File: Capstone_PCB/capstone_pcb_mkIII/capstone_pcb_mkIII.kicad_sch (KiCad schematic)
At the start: 18 parts, among them J1 DISPLAY_HEADER, J2 UART_TX, J3 UART_RX, J4 GND, SW1 SW_Push, SW2 SW_Push, U1 TPS62125DSG

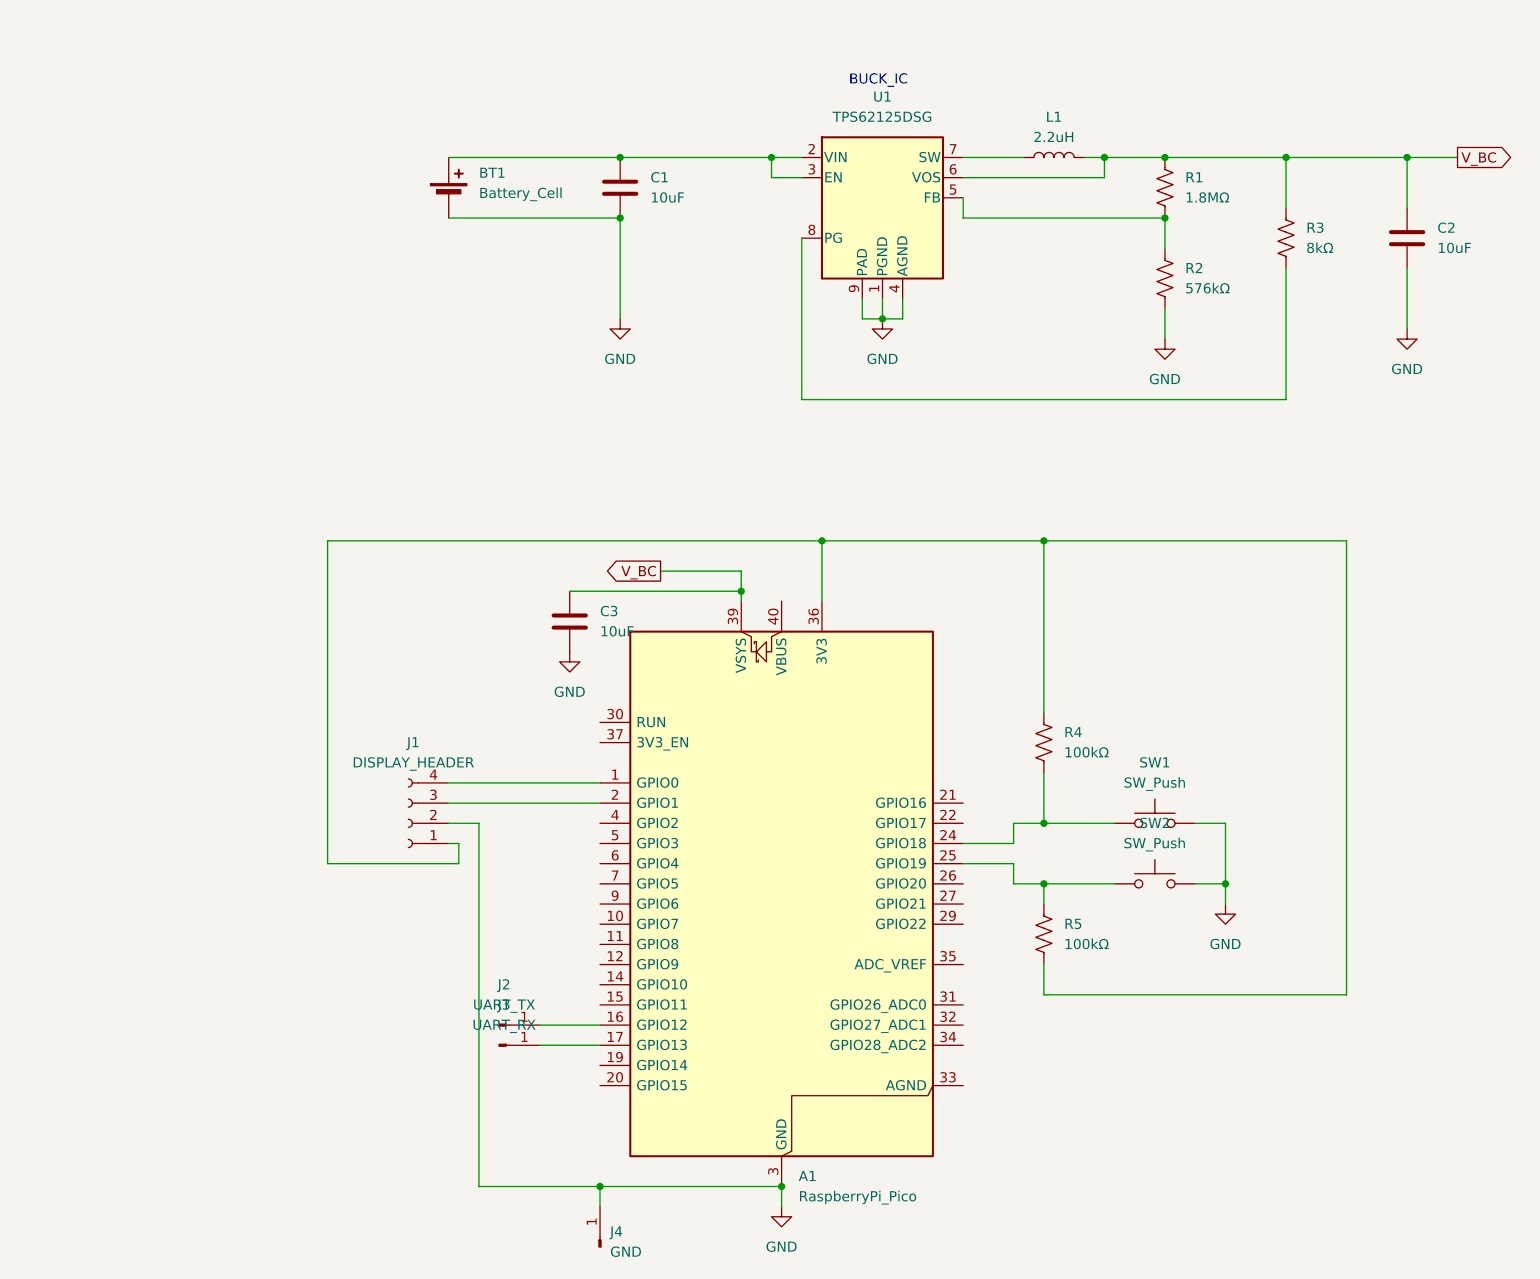
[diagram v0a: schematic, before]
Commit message: pcb almost done, few more errors to iron out tomorrow
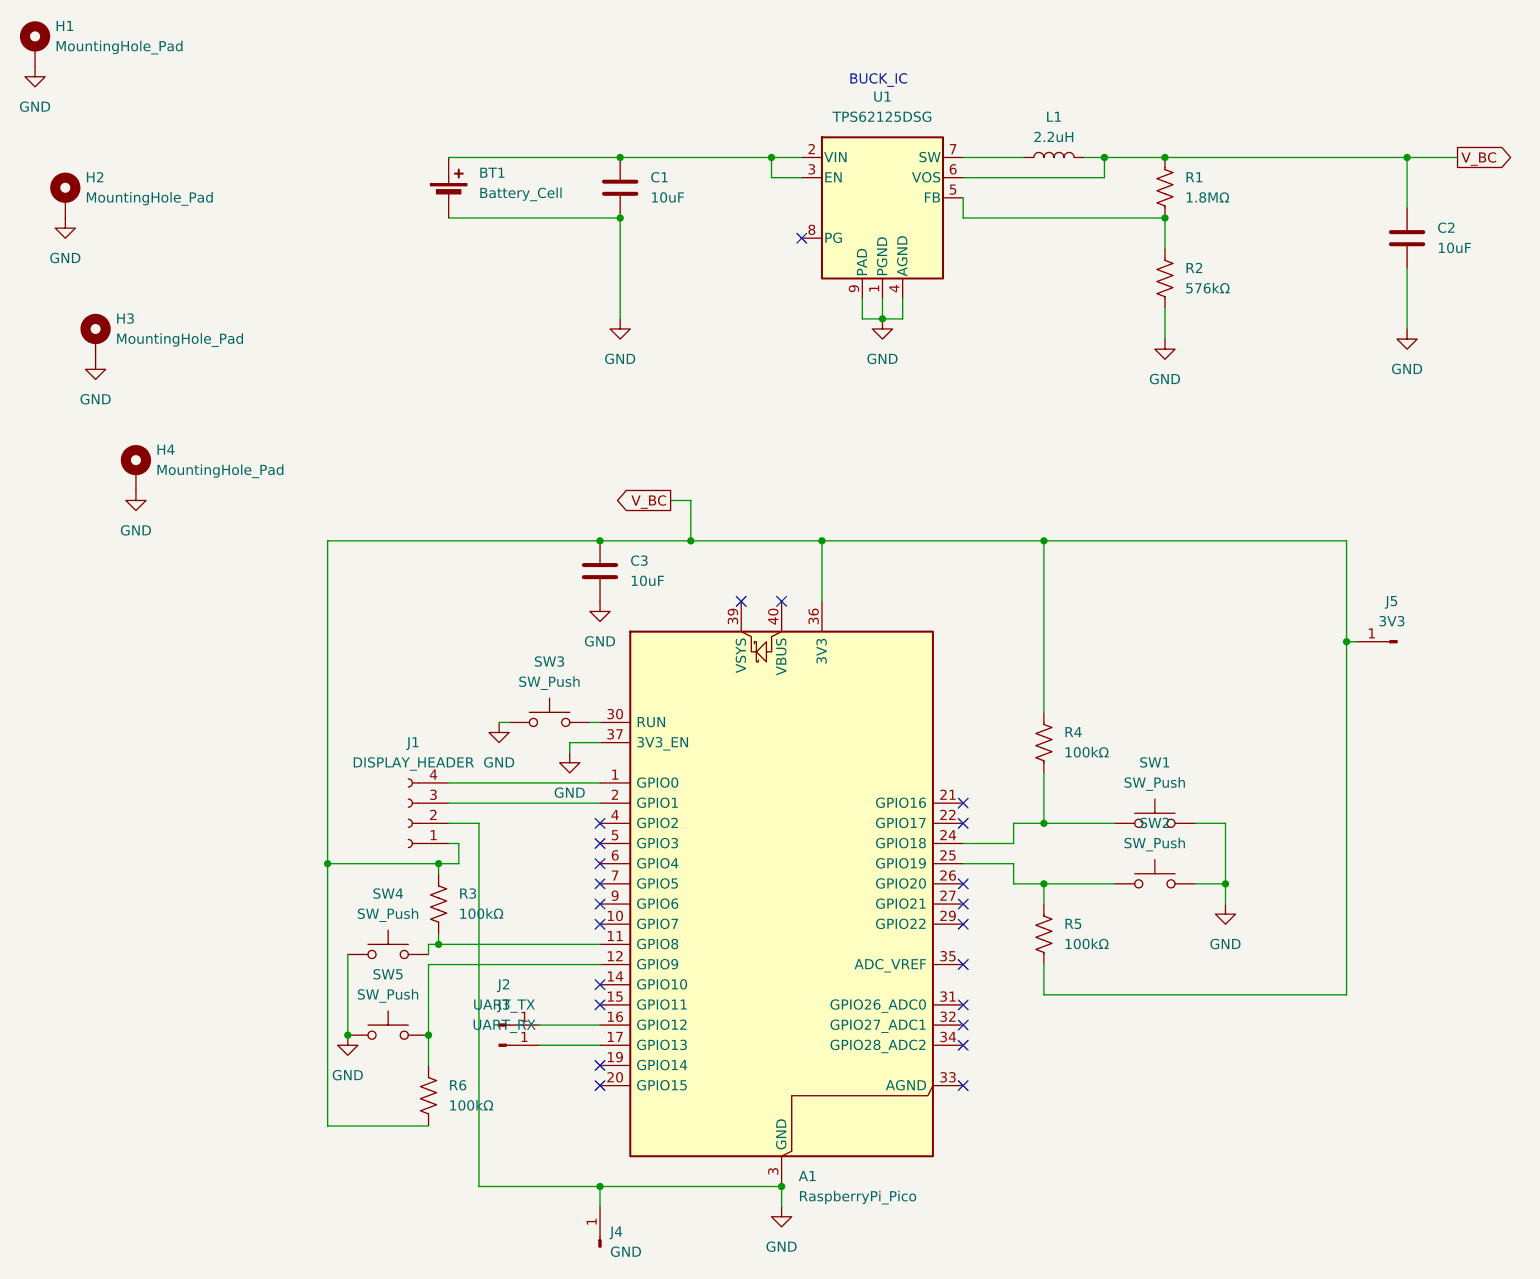
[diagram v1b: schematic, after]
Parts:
- added H1, H2, H3, H4: MountingHole_Pad, MountingHole:MountingHole_3.2mm_M3_Pad, symbol Mechanical:MountingHole_Pad
- added J5: 3V3, Connector_PinSocket_2.54mm:PinSocket_1x01_P2.54mm_Vertical, symbol Connector:Conn_01x01_Pin
- added R6: 100kΩ, Resistor_SMD:R_0603_1608Metric, symbol Device:R_US
- added SW3, SW4, SW5: SW_Push, Button_Switch_SMD:SW_SPST_Omron_B3FS-100xP, symbol Switch:SW_Push
- J1: footprint Connector_PinSocket_2.54mm:PinSocket_1x04_P2.54mm_Vertical_SMD_Pin1Right -> Connector_PinSocket_2.54mm:PinSocket_1x04_P2.54mm_Vertical
- R3: value 8kΩ -> 100kΩ
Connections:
- net GND: now also A1.37 (3V3_EN), H1.1, H2.1, H3.1, H4.1, SW3.1, SW4.1, SW5.1
- net V_BC: now also A1.36 (3V3), J1.1 (Pin_1), R3.2, R4.2, R5.1, J5.1 (Pin_1), R6.1; no longer A1.39 (VSYS), R3.1
- net at A1.11 (GPIO8): now also R3.1, SW4.2
- net at A1.12 (GPIO9): now also R6.2, SW5.2
- net at A1.30 (RUN): now also SW3.2
- net at U1.8 (PG): no longer R3.2
- no-connect marks 0 -> 23
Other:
- moved on the sheet: C3
